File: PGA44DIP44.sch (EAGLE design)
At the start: 2 parts, among them IC1 DIP44, IC2 PGA44

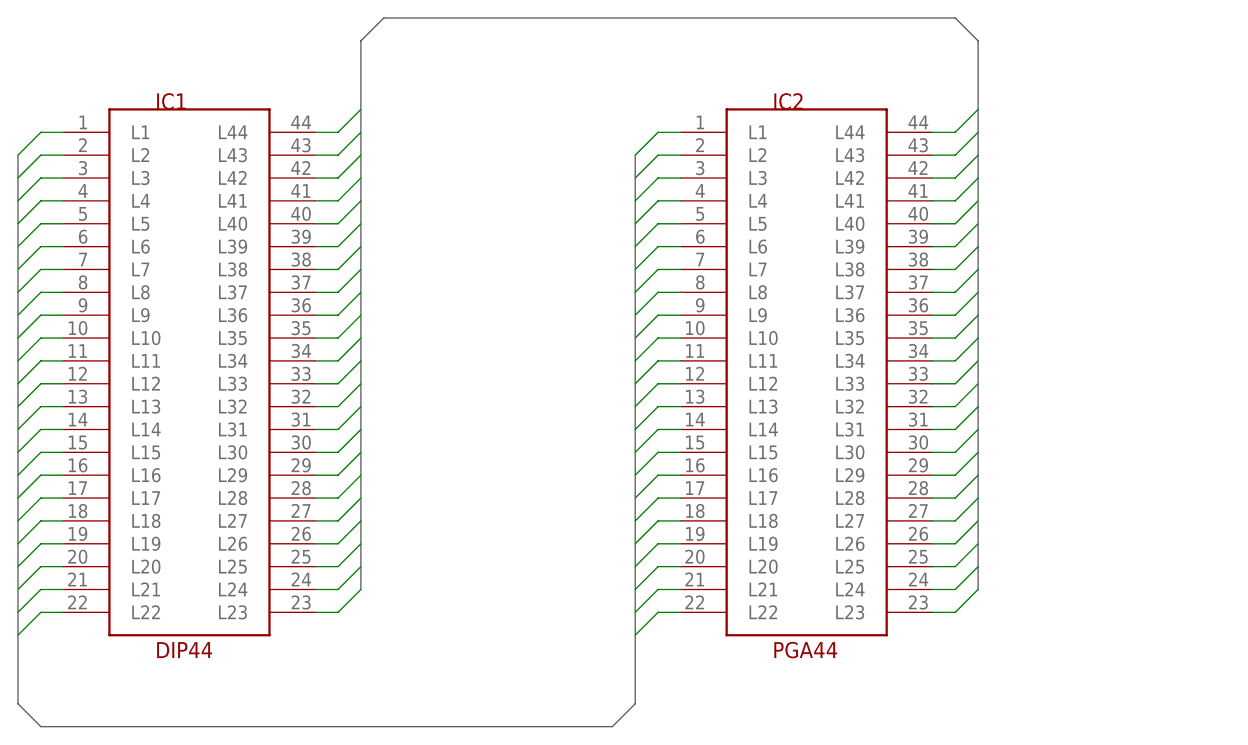
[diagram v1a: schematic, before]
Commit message: * Add smd jumper for XC95 usages. * Add jumper for XC95 commonly VCC usage. * Add gerber output.
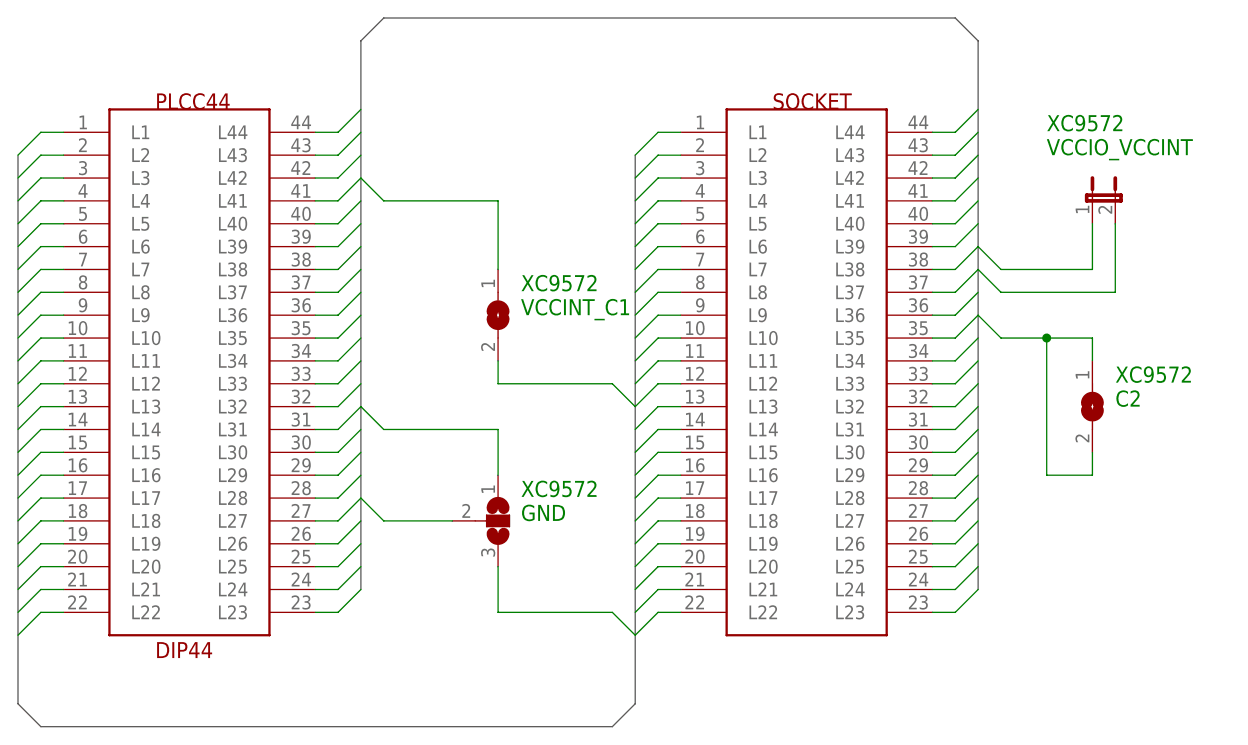
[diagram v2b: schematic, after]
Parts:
- added 　: (no value), jumper:JP1E
- added 　　: (no value), jumper:SJ
- added 　　　: (no value), jumper:SJ2W
- added 　　　　: (no value), jumper:SJ
- SOCKET: value PGA44 -> (none)
- renumbered IC1 to PLCC44, IC2 to SOCKET
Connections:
- net L10: now also 　　　.3
- net L21: now also 　　.2
- net L23: now also 　　　.1
- net L31: now also 　　　.2
- net L32: now also 　.1, 　　　　.1, 　　　　.2
- net L41: now also 　.2, 　　.1
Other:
- note added: "XC9572 C2"
- note added: "XC9572 GND"
- note added: "XC9572 VCCINT_C1"
- note added: "XC9572 VCCIO_VCCINT"

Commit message: Add XC95 features.
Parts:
- 　: device jumper:JP1E -> PGA44DIP44:JP1E
- 　　: device jumper:SJ -> PGA44DIP44:SJ
- 　　　: device jumper:SJ2W -> PGA44DIP44:SJ2W
- 　　　　: device jumper:SJ -> PGA44DIP44:SJ
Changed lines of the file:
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@@
 <part name="PLCC44" library="PGA44DIP44" deviceset="DIP44" device="" value="DIP44"/>
 <part name="SOCKET" library="PGA44DIP44" deviceset="PGA44" device=""/>
-<part name="　" library="jumper" deviceset="JP1E" device=""/>
-<part name="　　" library="jumper" deviceset="SJ" device=""/>
-<part name="　　　" library="jumper" deviceset="SJ2W" device=""/>
-<part name="　　　　" library="jumper" deviceset="SJ" device=""/>
+<part name="　" library="PGA44DIP44" deviceset="JP1E" device=""/>
+<part name="　　" library="PGA44DIP44" deviceset="SJ" device=""/>
+<part name="　　　" library="PGA44DIP44" deviceset="SJ2W" device=""/>
+<part name="　　　　" library="PGA44DIP44" deviceset="SJ" device=""/>
 </parts>
 <sheets>

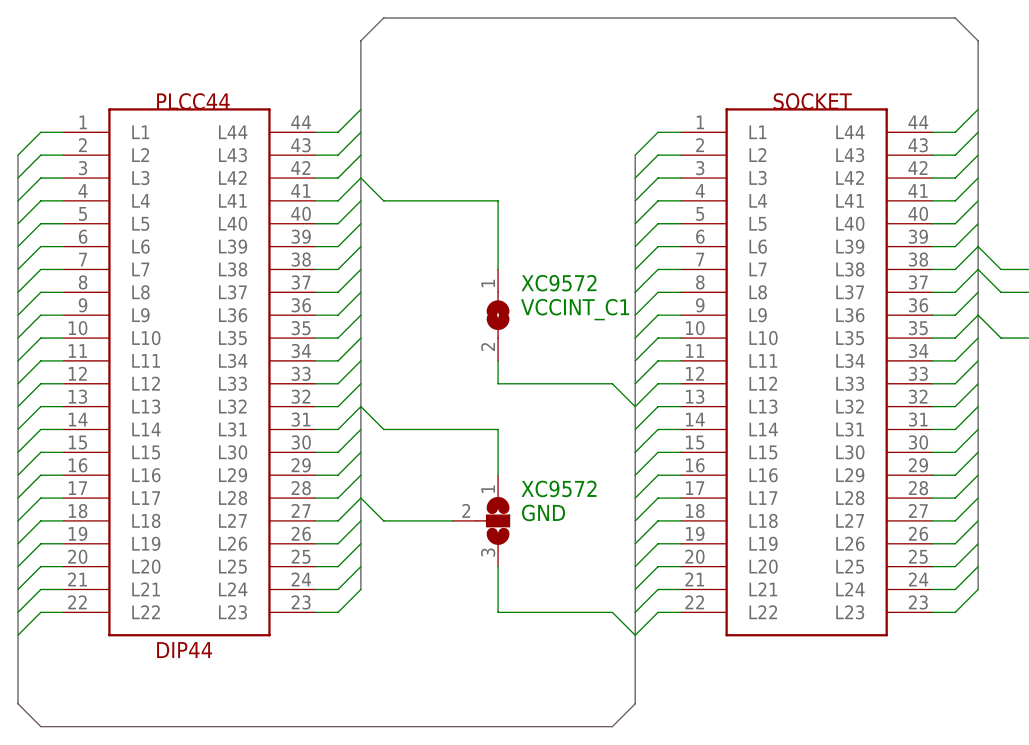
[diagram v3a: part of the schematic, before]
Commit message: * Fatal misassignment fixed for PGA44. * Update to EAGLE 8.1.0
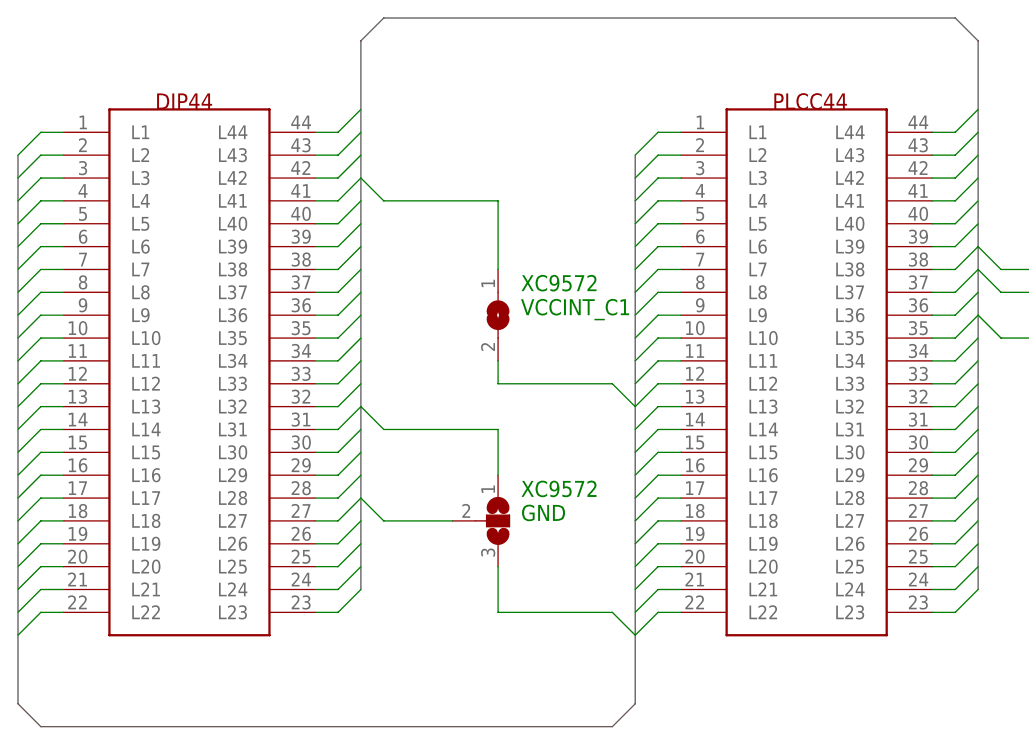
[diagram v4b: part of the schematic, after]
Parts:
- removed SOCKET: (no value), PGA44DIP44:PGA44
- added DIP44: DIP44, PGA44DIP44:DIP44
- PLCC44: value DIP44 -> PGA44; device PGA44DIP44:DIP44 -> PGA44DIP44:PGA44
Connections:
- net L1: now also DIP44.L1; no longer SOCKET.L1
- net L10: now also DIP44.L10; no longer SOCKET.L10
- net L11: now also DIP44.L11; no longer SOCKET.L11
- net L12: now also DIP44.L12; no longer SOCKET.L12
- net L13: now also DIP44.L13; no longer SOCKET.L13
- net L14: now also DIP44.L14; no longer SOCKET.L14
- net L15: now also DIP44.L15; no longer SOCKET.L15
- net L16: now also DIP44.L16; no longer SOCKET.L16
- net L17: now also DIP44.L17; no longer SOCKET.L17
- net L18: now also DIP44.L18; no longer SOCKET.L18
- net L19: now also DIP44.L19; no longer SOCKET.L19
- net L2: now also DIP44.L2; no longer SOCKET.L2
- net L20: now also DIP44.L20; no longer SOCKET.L20
- net L21: now also DIP44.L21; no longer SOCKET.L21
- net L22: now also DIP44.L22; no longer SOCKET.L22
- net L23: now also DIP44.L23; no longer SOCKET.L23
- net L24: now also DIP44.L24; no longer SOCKET.L24
- net L25: now also DIP44.L25; no longer SOCKET.L25
- net L26: now also DIP44.L26; no longer SOCKET.L26
- net L27: now also DIP44.L27; no longer SOCKET.L27
- net L28: now also DIP44.L28; no longer SOCKET.L28
- net L29: now also DIP44.L29; no longer SOCKET.L29
- net L3: now also DIP44.L3; no longer SOCKET.L3
- net L30: now also DIP44.L30; no longer SOCKET.L30
- net L31: now also DIP44.L31; no longer SOCKET.L31
- net L32: now also DIP44.L32; no longer SOCKET.L32
- net L33: now also DIP44.L33; no longer SOCKET.L33
- net L34: now also DIP44.L34; no longer SOCKET.L34
- net L35: now also DIP44.L35; no longer SOCKET.L35
- net L36: now also DIP44.L36; no longer SOCKET.L36
- net L37: now also DIP44.L37; no longer SOCKET.L37
- net L38: now also DIP44.L38; no longer SOCKET.L38
- net L39: now also DIP44.L39; no longer SOCKET.L39
- net L4: now also DIP44.L4; no longer SOCKET.L4
- net L40: now also DIP44.L40; no longer SOCKET.L40
- net L41: now also DIP44.L41; no longer SOCKET.L41
- net L42: now also DIP44.L42; no longer SOCKET.L42
- net L43: now also DIP44.L43; no longer SOCKET.L43
- net L44: now also DIP44.L44; no longer SOCKET.L44
- net L5: now also DIP44.L5; no longer SOCKET.L5
- net L6: now also DIP44.L6; no longer SOCKET.L6
- net L7: now also DIP44.L7; no longer SOCKET.L7
- net L8: now also DIP44.L8; no longer SOCKET.L8
- net L9: now also DIP44.L9; no longer SOCKET.L9
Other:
- moved on the sheet: PLCC44

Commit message: Fixed artworks.
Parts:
- removed 　: (no value), PGA44DIP44:JP1E
- removed 　　: (no value), PGA44DIP44:SJ
- removed 　　　: (no value), PGA44DIP44:SJ2W
- removed 　　　　: (no value), PGA44DIP44:SJ
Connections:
- net L10: no longer 　　　.3
- net L21: no longer 　　.2
- net L23: no longer 　　　.1
- net L31: no longer 　　　.2
- net L32: no longer 　.1, 　　　　.1, 　　　　.2
- net L41: no longer 　.2, 　　.1
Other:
- note removed: "XC9572 C2"
- note removed: "XC9572 GND"
- note removed: "XC9572 VCCINT_C1"
- note removed: "XC9572 VCCIO_VCCINT"
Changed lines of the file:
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@@
 <parts>
 <part name="DIP44" library="PGA44DIP44" deviceset="DIP44" device="" value="DIP44"/>
-<part name="　" library="PGA44DIP44" deviceset="JP1E" device=""/>
-<part name="　　" library="PGA44DIP44" deviceset="SJ" device=""/>
-<part name="　　　" library="PGA44DIP44" deviceset="SJ2W" device=""/>
-<part name="　　　　" library="PGA44DIP44" deviceset="SJ" device=""/>
 <part name="PLCC44" library="PGA44DIP44" deviceset="PGA44" device=""/>
 </parts>
@@
 <sheet>
 <plain>
-<text x="134.62" y="78.74" size="1.778" layer="91">XC9572
-VCCIO_VCCINT</text>
-<text x="76.2" y="60.96" size="1.778" layer="91">XC9572
-VCCINT_C1</text>
-<text x="76.2" y="38.1" size="1.778" layer="91">XC9572
-GND</text>
-<text x="142.24" y="50.8" size="1.778" layer="91">XC9572
-C2</text>
 </plain>
 <instances>
 <instance part="DIP44" gate="G$1" x="38.1" y="55.88"/>
-<instance part="　" gate="A" x="139.7" y="73.66"/>
-<instance part="　　" gate="1" x="73.66" y="60.96" rot="R270"/>
-<instance part="　　　" gate="G$1" x="73.66" y="38.1"/>
-<instance part="　　　　" gate="1" x="139.7" y="50.8" rot="R270"/>
 <instance part="PLCC44" gate="G$1" x="106.68" y="55.88"/>
 </instances>
@@
 <pinref part="PLCC44" gate="G$1" pin="L10"/>
 </segment>
-<segment>
-<wire x1="88.9" y1="25.4" x2="86.36" y2="27.94" width="0.1524" layer="91"/>
-<wire x1="86.36" y1="27.94" x2="73.66" y2="27.94" width="0.1524" layer="91"/>
-<pinref part="　　　" gate="G$1" pin="3"/>
-<wire x1="73.66" y1="27.94" x2="73.66" y2="33.02" width="0.1524" layer="91"/>
-</segment>
 </net>
 <net name="L11" class="0">
@@
 <pinref part="PLCC44" gate="G$1" pin="L21"/>
 </segment>
-<segment>
-<wire x1="88.9" y1="50.8" x2="86.36" y2="53.34" width="0.1524" layer="91"/>
-<wire x1="86.36" y1="53.34" x2="73.66" y2="53.34" width="0.1524" layer="91"/>
-<pinref part="　　" gate="1" pin="2"/>
-<wire x1="73.66" y1="53.34" x2="73.66" y2="55.88" width="0.1524" layer="91"/>
-</segment>
 </net>
 <net name="L22" class="0">
@@
 <pinref part="PLCC44" gate="G$1" pin="L23"/>
 </segment>
-<segment>
-<wire x1="58.42" y1="50.8" x2="60.96" y2="48.26" width="0.1524" layer="91"/>
-<wire x1="60.96" y1="48.26" x2="73.66" y2="48.26" width="0.1524" layer="91"/>
-<pinref part="　　　" gate="G$1" pin="1"/>
-<wire x1="73.66" y1="48.26" x2="73.66" y2="43.18" width="0.1524" layer="91"/>
-</segment>
 </net>
 <net name="L24" class="0">
@@
 <pinref part="PLCC44" gate="G$1" pin="L31"/>
 </segment>
-<segment>
-<wire x1="58.42" y1="40.64" x2="60.96" y2="38.1" width="0.1524" layer="91"/>
-<pinref part="　　　" gate="G$1" pin="2"/>
-<wire x1="60.96" y1="38.1" x2="68.58" y2="38.1" width="0.1524" layer="91"/>
-</segment>
 </net>
 <net name="L32" class="0">
@@
 <pinref part="PLCC44" gate="G$1" pin="L32"/>
 </segment>
-<segment>
-<wire x1="127" y1="68.58" x2="129.54" y2="66.04" width="0.1524" layer="91"/>
-<wire x1="129.54" y1="66.04" x2="139.7" y2="66.04" width="0.1524" layer="91"/>
-<pinref part="　" gate="A" pin="1"/>
-<wire x1="139.7" y1="66.04" x2="139.7" y2="71.12" width="0.1524" layer="91"/>
-</segment>
-<segment>
-<wire x1="127" y1="60.96" x2="129.54" y2="58.42" width="0.1524" layer="91"/>
-<wire x1="129.54" y1="58.42" x2="134.62" y2="58.42" width="0.1524" layer="91"/>
-<pinref part="　　　　" gate="1" pin="1"/>
-<wire x1="134.62" y1="58.42" x2="139.7" y2="58.42" width="0.1524" layer="91"/>
-<wire x1="139.7" y1="58.42" x2="139.7" y2="55.88" width="0.1524" layer="91"/>
-<wire x1="134.62" y1="58.42" x2="134.62" y2="43.18" width="0.1524" layer="91"/>
-<junction x="134.62" y="58.42"/>
-<wire x1="134.62" y1="43.18" x2="139.7" y2="43.18" width="0.1524" layer="91"/>
-<pinref part="　　　　" gate="1" pin="2"/>
-<wire x1="139.7" y1="43.18" x2="139.7" y2="45.72" width="0.1524" layer="91"/>
-</segment>
 </net>
 <net name="L33" class="0">
@@
 <wire x1="124.46" y1="73.66" x2="121.92" y2="73.66" width="0.1524" layer="91"/>
 <pinref part="PLCC44" gate="G$1" pin="L41"/>
-</segment>
-<segment>
-<wire x1="127" y1="66.04" x2="129.54" y2="63.5" width="0.1524" layer="91"/>
-<wire x1="129.54" y1="63.5" x2="142.24" y2="63.5" width="0.1524" layer="91"/>
-<pinref part="　" gate="A" pin="2"/>
-<wire x1="142.24" y1="63.5" x2="142.24" y2="71.12" width="0.1524" layer="91"/>
-</segment>
-<segment>
-<wire x1="58.42" y1="76.2" x2="60.96" y2="73.66" width="0.1524" layer="91"/>
-<wire x1="60.96" y1="73.66" x2="73.66" y2="73.66" width="0.1524" layer="91"/>
-<pinref part="　　" gate="1" pin="1"/>
-<wire x1="73.66" y1="73.66" x2="73.66" y2="66.04" width="0.1524" layer="91"/>
 </segment>
 </net>
@@
 </schematic>
 </drawing>
-<compatibility>
-<note version="6.3" minversion="6.2.2" severity="warning">
-Since Version 6.2.2 text objects can contain more than one line,
-which will not be processed correctly with this version.
-</note>
-</compatibility>
 </eagle>

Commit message: Gerber data move into sub directory.
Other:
- note added: "https://github.com/kekyo/PGA44DIP44 CC BY-NC-SA 4.0"
- moved on the sheet: DIP44, PLCC44

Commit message: Artwork predesigning (WIP)
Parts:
- added C1, C2, C3, C4: 0.1uF, rcl:C-US050-024X044
- added CN1: JTAG, con-lsta:FE05-1
- added IC1: LM2937ET-3.3/NOPB, PGA44DIP44:LM2937ET-3.3/NOPB
- added JP1: (no value), PGA44DIP44:JP1E
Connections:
- new net GND: C1.2, C2.2, C3.2, C4.2, CN1.5, IC1.GND
- new net N$1: IC1.OUT, JP1.1
- new net VCCINT: C3.1, C4.1, JP1.2
- new net VCCIO: C1.1, C2.1, IC1.IN
- net L15: now also CN1.4
- net L16: now also CN1.1
- net L17: now also CN1.2
- net L30: now also CN1.3
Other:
- note added: "TCK"
- note added: "TDI"
- note added: "TDO"
- note added: "TMS"
- moved on the sheet: DIP44, PLCC44
